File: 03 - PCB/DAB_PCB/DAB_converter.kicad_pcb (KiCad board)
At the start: 2 copper layers, 163.5 x 128 mm, 173 parts, among them IC1 UCC27288DR, IC10 INA201AID, IC11 INA201AID, IC12 MCP6241-E_P, IC13 MCP6241-E_P, IC2 UCC27288DR, IC3 UCC27288DR, IC4 UCC27288DR, IC5 UA78L12ACDR, IC6 INA201AID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

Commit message: started routing
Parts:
- added TP1: Vds1, DAB:test point 2, F.Cu at (137.5, 42.5)
- added TP10: sec, DAB:test point 2, F.Cu at (48.0, 149.5)
- added TP11: ac, DAB:test point 2, F.Cu at (134.0, 96.0)
- added TP12: TP?, Connector_PinHeader_2.54mm:PinHeader_1x03_P2.54mm_Vertical, F.Cu at (167.5, 130.0)
- added TP13: Vaux, DAB:test point 2, F.Cu at (175.5, 130.0)
- added TP14: I'', DAB:test point 2, F.Cu at (62.5, 122.5)
- added TP15: I_ac, DAB:test point 2, F.Cu at (68.5, 103.2)
- added TP16: V'', DAB:test point 2, F.Cu at (51.5, 133.7)
- added TP17: Conn_01x10_Pin, Connector_PinHeader_2.54mm:PinHeader_1x10_P2.54mm_Vertical, F.Cu at (18.0, 103.0)
- added TP18: TP?, Connector_PinHeader_2.54mm:PinHeader_1x03_P2.54mm_Vertical, F.Cu at (91.5, 63.9)
- added TP19: V', DAB:test point 2, F.Cu at (45.5, 71.5)
- added TP2: Vds3, DAB:test point 2, F.Cu at (138.5, 88.0)
- added TP20: I', DAB:test point 2, F.Cu at (53.0, 71.5)
- added TP3: Vds5, DAB:test point 2, F.Cu at (137.2, 118.5)
- added TP4: Vds7, DAB:test point 2, F.Cu at (137.2, 146.5)
- added TP5: Vgs2, DAB:test point 2, F.Cu at (137.2, 60.0)
- added TP6: Vgs4, DAB:test point 2, F.Cu at (128.5, 87.7)
- added TP7: Vgs6, DAB:test point 2, F.Cu at (139.5, 123.0)
- added TP8: Vgs8, DAB:test point 2, F.Cu at (137.5, 150.5)
- added TP9: prim, DAB:test point 2, F.Cu at (56.2, 40.5)
- moved G*** 61.5 mm to (52.0, 157.0)
- moved C10 21.0 mm to (66.5, 74.0)
- moved C9 21.0 mm to (70.0, 74.0)
- moved C4 16.0 mm to (83.0, 73.9)
- moved C5 16.0 mm to (86.5, 73.9)
- moved C8 16.0 mm to (89.7, 74.0)
- moved R17 14.6 mm to (48.5, 56.5)
- moved C19 12.6 mm to (35.5, 80.5)
- moved R20 12.6 mm to (39.5, 79.0)
- moved C18 9.62 mm to (35.5, 91.0)
- moved R19 9.55 mm to (39.5, 89.5)
- moved C_vdd6 7.16 mm to (63.0, 130.5), turned to 90 degrees
- moved C_fil1 6.52 mm to (104.5, 95.5)
- moved C_vdd7 6.52 mm to (57.0, 68.0), turned to 180 degrees
- moved Rfil1 6.39 mm to (110.0, 97.5)
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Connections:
- net Net-(IC10-OUT) renamed /I'
- net Net-(IC11-OUT) renamed /I''
- net Net-(IC12-VOUT) renamed /V'
- net Net-(IC13-VOUT) renamed /V''
- C16 pad 2: /ADCA2 -> /ADCA3
- C18 pad 2: /ADCA2 -> /ADCA3
- C21 pad 2: /prim+ -> /prim-
- C22 pad 2: /prim+ -> /prim-
- PS1 pad 1: /prim+ -> /prim-
- R15 pad 1: /ADCA2 -> /ADCA3
- R19 pad 2: /ADCA2 -> /ADCA3
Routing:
- net /prim-: track 0.00 -> 151.6 mm
- net /PWM4A_ISO: track 0.00 -> 105.0 mm, vias 0 -> 1
- net /PWM1A_ISO: track 0.00 -> 102.2 mm, vias 0 -> 1
- net /PWM4B_ISO: track 0.00 -> 97.3 mm, vias 0 -> 1
- net /PWM1B_ISO: track 0.00 -> 96.5 mm, vias 0 -> 1
- net /sec+: track 0.00 -> 92.0 mm, vias 1 -> 8
- net /PWM3A_ISO: track 0.00 -> 91.9 mm, vias 0 -> 1
- net /PWM2A_ISO: track 0.00 -> 90.0 mm, vias 0 -> 1
- net /PWM3B_ISO: track 0.00 -> 84.7 mm, vias 0 -> 1
- net /PWM2B_ISO: track 0.00 -> 83.7 mm, vias 0 -> 1
- net /vs5: track 0.00 -> 68.7 mm
- net Net-(D3-A): track 0.00 -> 67.2 mm, vias 0 -> 2
- net /ac+: track 0.00 -> 64.6 mm
- net /vs7: track 0.00 -> 64.4 mm
- net /V'': track 0.00 -> 62.4 mm
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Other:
- board text added: "Bregy Loris Luo Rubie"
- board text removed: "Bregy Loris - Luo Rubie"

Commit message: added all test points
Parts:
- added TP21: 2L, DAB:test point 2, F.Cu at (101.0, 90.5)
- added TP22: 3L, DAB:test point 2, F.Cu at (100.5, 120.5)
- added TP23: 4L, DAB:test point 2, F.Cu at (100.0, 151.0)
- added TP24: 1H, DAB:test point 2, F.Cu at (101.5, 61.5)
- added TP25: 2H, DAB:test point 2, F.Cu at (101.0, 86.5)
- added TP26: 3H, DAB:test point 2, F.Cu at (100.5, 124.5)
- added TP27: 4H, DAB:test point 2, F.Cu at (100.0, 147.0)
- TP17: value Conn_01x10_Pin -> 1L; footprint Connector_PinHeader_2.54mm:PinHeader_1x10_P2.54mm_Vertical -> DAB:test point 2
- moved TP17 91.7 mm to (101.5, 65.0), turned to -90 degrees
- moved Chi3 2.44 mm to (103.0, 143.6)
- moved Cli3 2.44 mm to (108.0, 143.6)
- moved Rhi3 2.44 mm to (104.0, 147.6)
- moved Rli3 2.44 mm to (107.0, 147.5)
- moved IC3 2.22 mm to (107.0, 138.0)
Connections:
- C18 pad 2: /ADCA3 -> /ADCA2
- R19 pad 2: /ADCA3 -> /ADCA2
- TP17 pad 1: GND -> /PWM1A_ISO
- TP17 pad 2: /PWM1A_ISO -> GND
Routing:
- net /PWM4B_ISO: track 97.3 -> 98.8 mm
- net /PWM2B_ISO: track 83.7 -> 85.0 mm
- net /PWM2A_ISO: track 90.0 -> 91.3 mm
- net /PWM3B_ISO: track 84.7 -> 85.4 mm
- net /PWM3A_ISO: track 91.9 -> 92.6 mm
- net GND: vias 2 -> 0
- net 12Vpri: vias 6 -> 4

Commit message: more routing
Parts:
- moved TP2 16.5 mm to (138.5, 71.5)
- moved TP6 10.0 mm to (138.5, 88.0), turned to 90 degrees
- moved Rg2 1.51 mm to (130.5, 88.5)
- moved Rgs2 1.51 mm to (133.5, 88.5)
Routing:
- net /vs5: track 68.7 -> 107.6 mm
- net /sec+: track 92.0 -> 127.9 mm
- net /vs1: track 19.9 -> 52.4 mm
- net Net-(IC4-HO): track 0.00 -> 24.2 mm
- net Net-(IC2-LO): track 0.00 -> 24.2 mm
- net Net-(IC1-HO): track 0.00 -> 22.6 mm
- net Net-(IC2-HO): track 0.00 -> 22.6 mm
- net Net-(IC1-LO): track 0.00 -> 21.1 mm
- net /ac-: track 39.6 -> 59.7 mm
- net /vg5: track 0.00 -> 12.1 mm
- net /vg4: track 0.00 -> 12.0 mm
- net Net-(Dboot2-K): track 0.00 -> 12.0 mm
- net /vg1: track 0.00 -> 11.9 mm
- net /vg3: track 0.00 -> 10.9 mm
- net Net-(Dboot1-K): track 0.00 -> 9.65 mm
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
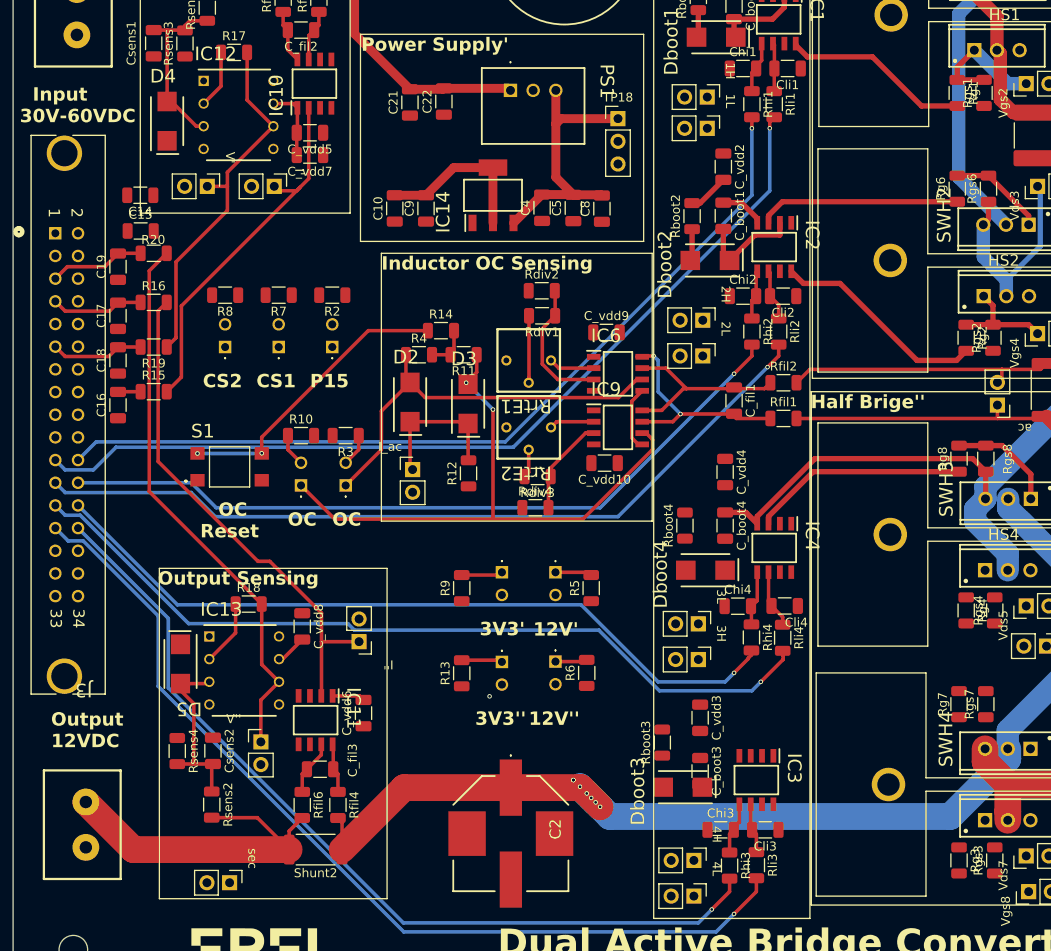
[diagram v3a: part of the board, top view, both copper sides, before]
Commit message: gate drivers routed
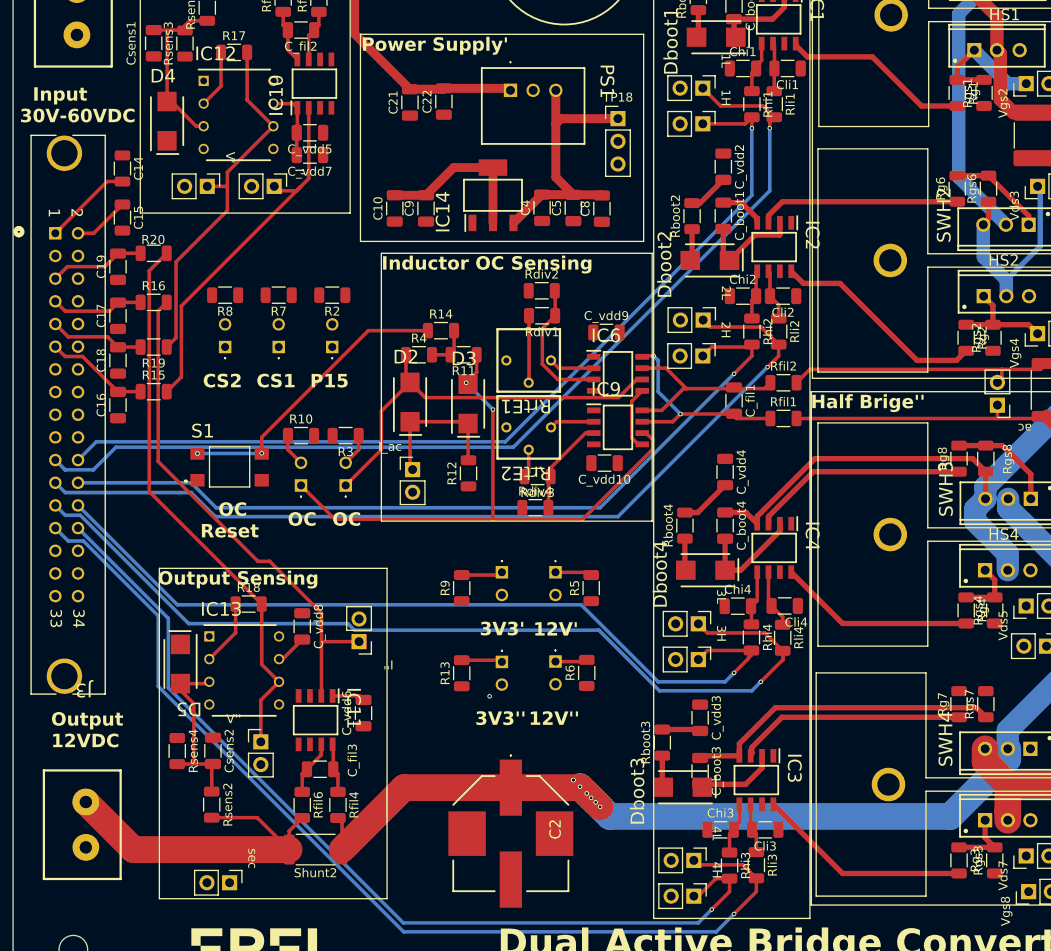
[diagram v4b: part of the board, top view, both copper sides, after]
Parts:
- moved TP17 4.53 mm to (101.0, 60.5)
- moved TP21 4.02 mm to (101.0, 86.5)
- moved TP23 4.00 mm to (100.0, 147.0)
- moved TP25 4.00 mm to (101.0, 90.5)
- moved TP27 4.00 mm to (100.0, 151.0)
- moved C14 3.61 mm to (36.0, 69.5), turned to -90 degrees
- moved TP24 3.04 mm to (101.0, 64.5)
- moved C15 2.53 mm to (36.0, 75.0), turned to -90 degrees
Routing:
- net /vs7: track 64.0 -> 99.6 mm
- net Net-(IC3-HO): track 0.00 -> 25.6 mm
- net Net-(IC3-LO): track 0.00 -> 24.0 mm
- net Net-(IC4-LO): track 0.00 -> 22.0 mm
- net Net-(Dboot4-K): track 0.00 -> 12.3 mm
- net /PWM3A_ISO: track 92.6 -> 103.3 mm
- net /ADCA2: track 0.00 -> 10.6 mm
- net 12Vpri: track 67.8 -> 77.8 mm
- net Net-(C14-Pad2): track 0.00 -> 9.92 mm
- net /PWM2A_ISO: track 91.3 -> 100.9 mm
- net /PWM1A_ISO: track 101.9 -> 111.2 mm
- net Net-(Dboot3-K): track 0.00 -> 9.05 mm
- net /PWM4A_ISO: track 105.2 -> 113.1 mm
- net /vg8: track 0.00 -> 7.48 mm
- net /vg6: track 0.00 -> 6.68 mm
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
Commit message: DC-DC
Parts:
- added G***: LOGO, DAB:DC-DC, B.Cu at (106.0, 98.0)
- moved R14 25.4 mm to (48.5, 98.0)
- moved TP10 6.50 mm to (54.5, 149.5)
- moved TP14 3.00 mm to (62.5, 125.5)
- moved TP6 2.78 mm to (141.3, 88.0), turned to -90 degrees
- moved TP7 2.38 mm to (137.2, 122.3), turned to 90 degrees
- moved Me3 1.50 mm to (30.5, 155.5)
- moved Rgs2 1.50 mm to (132.0, 88.5)
- moved TP15 1.32 mm to (68.0, 102.0)
- moved R12 1.15 mm to (74.8, 102.5)
- moved Rg2 1.00 mm to (129.5, 88.5)
- moved C_vdd6 0.50 mm to (63.0, 130.0)
- moved TP8 0.28 mm to (137.2, 150.5)
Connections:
- C11 pad 2: 12Vpri -> 12Vsec
- C6 pad 2: 12Vpri -> 12Vsec
- C_vdd3 pad 2: 12Vpri -> 12Vsec
- C_vdd4 pad 2: 12Vpri -> 12Vsec
- IC15 pad 3: 12Vpri -> 12Vsec
- IC3 pad 1: 12Vpri -> 12Vsec
- IC4 pad 1: 12Vpri -> 12Vsec
- IC5 pad 1: 12Vpri -> 12Vsec
- LED2 pad 2: 12Vpri -> 12Vsec
- Rboot3 pad 2: 12Vpri -> 12Vsec
- Rboot4 pad 2: 12Vpri -> 12Vsec
- TP12 pad 1: 12Vpri -> 12Vsec
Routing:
- net 12Vsec: track 0.00 -> 177.0 mm, vias 0 -> 6
- net 3V3pri: track 31.6 -> 205.8 mm, vias 0 -> 4
- net 3V3sec: track 30.6 -> 178.9 mm, vias 0 -> 2
- net 12Vpri: track 77.8 -> 152.4 mm, vias 0 -> 6
- net /ECAP2_ISO: track 16.2 -> 65.2 mm, vias 0 -> 1
- net /ac-: track 59.7 -> 97.5 mm
- net /GPIO15_ISO: track 0.00 -> 28.8 mm, vias 0 -> 1
- net Net-(IC6-~{RESET}): track 39.8 -> 64.2 mm
- net /CS1_ISO: track 0.00 -> 22.7 mm, vias 0 -> 1
- net /CS2_ISO: track 0.00 -> 17.1 mm, vias 0 -> 1
- net /vg7: track 0.00 -> 13.2 mm
- net /prim+: track 32.0 -> 41.8 mm
- net /vs7: track 99.6 -> 108.0 mm
- net /sec+: track 127.9 -> 135.5 mm, vias 8 -> 7
- net /prim-: track 151.6 -> 158.4 mm
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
